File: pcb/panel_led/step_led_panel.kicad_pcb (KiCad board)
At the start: 2 copper layers, 228.6 x 76.2 mm, 46 parts, among them J1 Screw_Terminal_01x03, J2 Screw_Terminal_01x03, J3 Screw_Terminal_01x02

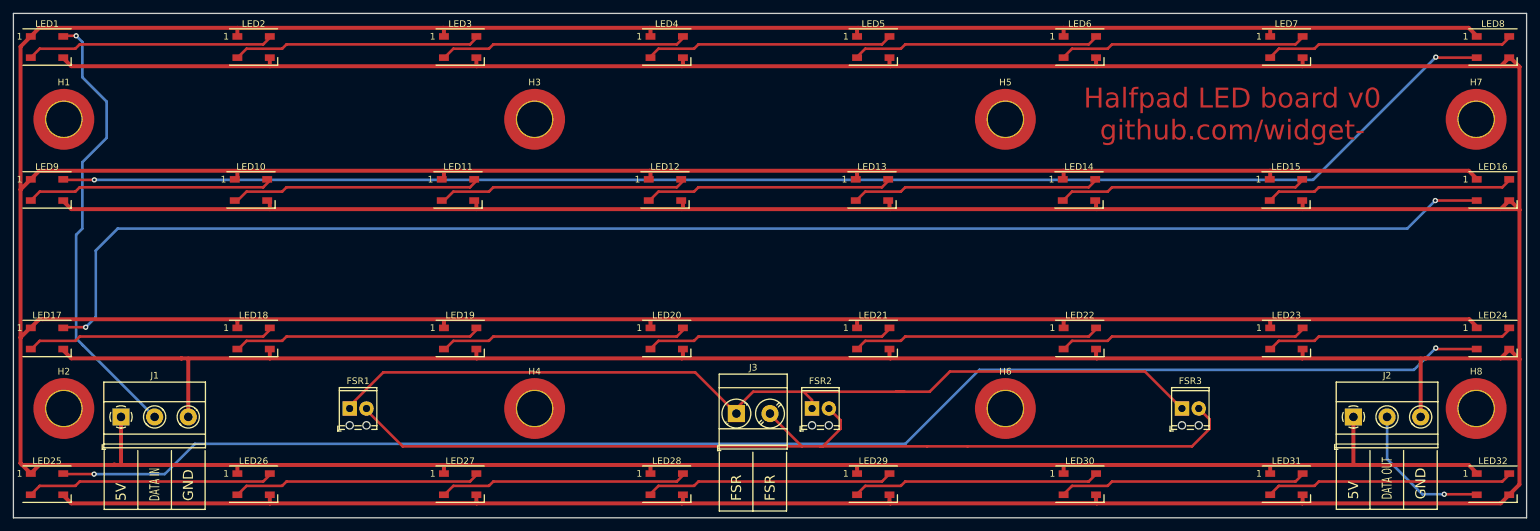
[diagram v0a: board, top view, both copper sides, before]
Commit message: Finalize v0.1 of breakout board to start v0.2
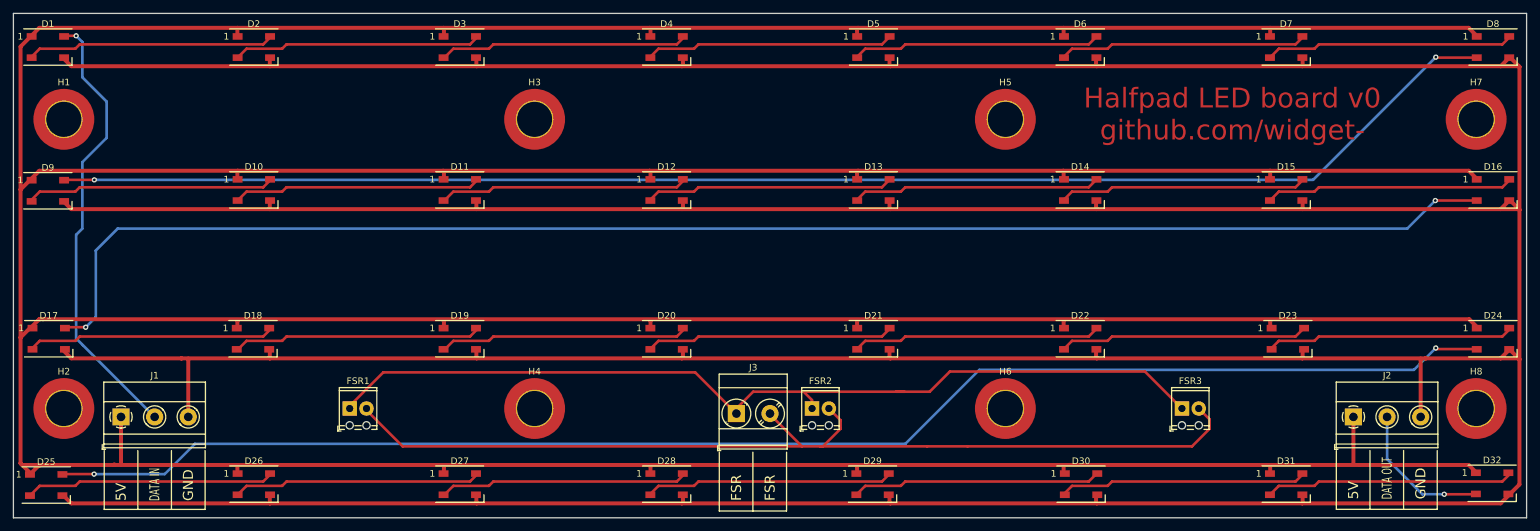
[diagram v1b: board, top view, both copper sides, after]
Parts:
- removed LED1, LED10, LED11, LED12, LED13, LED14, LED15, LED16, LED17, LED18, LED19, LED2, LED20, LED21, LED22, LED23, LED24, LED25, LED26, LED27, LED28, LED29, LED3, LED30, LED31, LED32, LED4, LED5, LED6, LED7, LED8, LED9: WS2812B, LED_SMD:LED_WS2812B_PLCC4_5.0x5.0mm_P3.2mm
- added D1: WS2812, LED_SMD:LED_WS2812B_PLCC4_5.0x5.0mm_P3.2mm, F.Cu at (5.21, 5.08)
- added D10: WS2812, LED_SMD:LED_WS2812B_PLCC4_5.0x5.0mm_P3.2mm, F.Cu at (36.3, 26.7)
- added D11: WS2812, LED_SMD:LED_WS2812B_PLCC4_5.0x5.0mm_P3.2mm, F.Cu at (67.4, 26.7)
- added D12: WS2812, LED_SMD:LED_WS2812B_PLCC4_5.0x5.0mm_P3.2mm, F.Cu at (98.7, 26.7)
- added D13: WS2812, LED_SMD:LED_WS2812B_PLCC4_5.0x5.0mm_P3.2mm, F.Cu at (129.9, 26.7)
- added D14: WS2812, LED_SMD:LED_WS2812B_PLCC4_5.0x5.0mm_P3.2mm, F.Cu at (161.2, 26.7)
- added D15: WS2812, LED_SMD:LED_WS2812B_PLCC4_5.0x5.0mm_P3.2mm, F.Cu at (192.3, 26.7)
- added D16: WS2812, LED_SMD:LED_WS2812B_PLCC4_5.0x5.0mm_P3.2mm, F.Cu at (223.5, 26.7)
- added D17: WS2812, LED_SMD:LED_WS2812B_PLCC4_5.0x5.0mm_P3.2mm, F.Cu at (5.33, 49.1)
- added D18: WS2812, LED_SMD:LED_WS2812B_PLCC4_5.0x5.0mm_P3.2mm, F.Cu at (36.2, 49.1)
- added D19: WS2812, LED_SMD:LED_WS2812B_PLCC4_5.0x5.0mm_P3.2mm, F.Cu at (67.4, 49.1)
- added D2: WS2812, LED_SMD:LED_WS2812B_PLCC4_5.0x5.0mm_P3.2mm, F.Cu at (36.3, 5.08)
- added D20: WS2812, LED_SMD:LED_WS2812B_PLCC4_5.0x5.0mm_P3.2mm, F.Cu at (98.7, 49.1)
- added D21: WS2812, LED_SMD:LED_WS2812B_PLCC4_5.0x5.0mm_P3.2mm, F.Cu at (129.9, 49.1)
- added D22: WS2812, LED_SMD:LED_WS2812B_PLCC4_5.0x5.0mm_P3.2mm, F.Cu at (161.2, 49.1)
- added D23: WS2812, LED_SMD:LED_WS2812B_PLCC4_5.0x5.0mm_P3.2mm, F.Cu at (192.5, 49.1)
- added D24: WS2812, LED_SMD:LED_WS2812B_PLCC4_5.0x5.0mm_P3.2mm, F.Cu at (223.5, 49.1)
- added D25: WS2812, LED_SMD:LED_WS2812B_PLCC4_5.0x5.0mm_P3.2mm, F.Cu at (4.95, 71.2)
- added D26: WS2812, LED_SMD:LED_WS2812B_PLCC4_5.0x5.0mm_P3.2mm, F.Cu at (36.3, 71.1)
- added D27: WS2812, LED_SMD:LED_WS2812B_PLCC4_5.0x5.0mm_P3.2mm, F.Cu at (67.4, 71.1)
- added D28: WS2812, LED_SMD:LED_WS2812B_PLCC4_5.0x5.0mm_P3.2mm, F.Cu at (98.7, 71.1)
- added D29: WS2812, LED_SMD:LED_WS2812B_PLCC4_5.0x5.0mm_P3.2mm, F.Cu at (129.8, 71.1)
- added D3: WS2812, LED_SMD:LED_WS2812B_PLCC4_5.0x5.0mm_P3.2mm, F.Cu at (67.4, 5.08)
- added D30: WS2812, LED_SMD:LED_WS2812B_PLCC4_5.0x5.0mm_P3.2mm, F.Cu at (161.3, 71.1)
- added D31: WS2812, LED_SMD:LED_WS2812B_PLCC4_5.0x5.0mm_P3.2mm, F.Cu at (192.3, 71.1)
- added D32: WS2812, LED_SMD:LED_WS2812B_PLCC4_5.0x5.0mm_P3.2mm, F.Cu at (223.4, 71.0)
- added D4: WS2812, LED_SMD:LED_WS2812B_PLCC4_5.0x5.0mm_P3.2mm, F.Cu at (98.7, 5.08)
- added D5: WS2812, LED_SMD:LED_WS2812B_PLCC4_5.0x5.0mm_P3.2mm, F.Cu at (129.9, 5.08)
- added D6: WS2812, LED_SMD:LED_WS2812B_PLCC4_5.0x5.0mm_P3.2mm, F.Cu at (161.2, 5.08)
- added D7: WS2812, LED_SMD:LED_WS2812B_PLCC4_5.0x5.0mm_P3.2mm, F.Cu at (192.3, 5.08)
- added D8: WS2812, LED_SMD:LED_WS2812B_PLCC4_5.0x5.0mm_P3.2mm, F.Cu at (223.5, 5.08)
- added D9: WS2812, LED_SMD:LED_WS2812B_PLCC4_5.0x5.0mm_P3.2mm, F.Cu at (5.21, 26.8)
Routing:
- net Net-(LED16-Pad2): track 227.3 -> 0.00 mm, vias 2 -> 0
- net Net-(D16-Pad2): track 0.00 -> 227.3 mm, vias 0 -> 2
- net Net-(LED24-Pad2): track 221.4 -> 0.00 mm, vias 2 -> 0
- net Net-(D24-Pad2): track 0.00 -> 221.4 mm, vias 0 -> 2
- net Net-(LED8-Pad2): track 221.2 -> 0.00 mm, vias 2 -> 0
- net Net-(D8-Pad2): track 0.00 -> 221.2 mm, vias 0 -> 2
- net Net-(LED7-Pad2): track 37.5 -> 0.00 mm
- net Net-(LED6-Pad2): track 37.5 -> 0.00 mm
- net Net-(LED5-Pad2): track 37.5 -> 0.00 mm
- net Net-(LED4-Pad2): track 37.5 -> 0.00 mm
- net Net-(LED22-Pad2): track 37.5 -> 0.00 mm
- net Net-(LED20-Pad2): track 37.5 -> 0.00 mm
- net Net-(LED2-Pad2): track 37.5 -> 0.00 mm
- net Net-(LED17-Pad2): track 37.5 -> 0.00 mm
- net Net-(D7-Pad2): track 0.00 -> 37.5 mm
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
